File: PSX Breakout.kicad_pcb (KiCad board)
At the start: 2 copper layers, 100 x 51.8 mm, 28 parts, among them J1 Conn_01x12_Male, J2 Mini-DIN-4, J3 VAL**, J4 DB15_Female_HighDensity, J5 3x2_RCA, SW1 SW_SPDT, SW2 SW_SP3T, SW3 SW_SP3T, U1 LM1881

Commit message: Fixed Gerbers, added footprints
Updated gerbers, and added all footprints used on this board to the PSX_BREAKOUT.Pretty folder.
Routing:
- net Net-(C5-Pad1): track 84.7 -> 94.5 mm
- net GND: vias 30 -> 31
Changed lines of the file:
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@@
     (thickness 1.6)
     (drawings 18)
-    (tracks 332)
+    (tracks 334)
     (zones 0)
     (modules 28)
@@
   (page A4)
   (layers
-    (0 F.Cu signal hide)
-    (31 B.Cu signal hide)
+    (0 F.Cu signal)
+    (31 B.Cu signal)
     (32 B.Adhes user)
     (33 F.Adhes user)
@@
   (segment (start 115.443 95.377) (end 107.815 95.377) (width 0.25) (layer F.Cu) (net 8))
   (via (at 179.705 75.946) (size 0.8) (drill 0.4) (layers F.Cu B.Cu) (net 9))
-  (segment (start 124.883 86.233) (end 123.858 86.233) (width 0.25) (layer F.Cu) (net 9))
-  (segment (start 126.122 86.233) (end 124.883 86.233) (width 0.25) (layer F.Cu) (net 9))
-  (segment (start 128.513 88.624) (end 126.122 86.233) (width 0.25) (layer F.Cu) (net 9))
-  (segment (start 129.413 88.624) (end 128.513 88.624) (width 0.25) (layer F.Cu) (net 9))
-  (segment (start 120.335 91.119) (end 120.335 91.694) (width 0.25) (layer F.Cu) (net 9))
-  (segment (start 120.335 88.731) (end 120.335 91.119) (width 0.25) (layer F.Cu) (net 9))
-  (segment (start 122.833 86.233) (end 120.335 88.731) (width 0.25) (layer F.Cu) (net 9))
-  (segment (start 123.858 86.233) (end 122.833 86.233) (width 0.25) (layer F.Cu) (net 9))
   (segment (start 120.335 93.331) (end 120.321 93.345) (width 0.25) (layer F.Cu) (net 9))
   (segment (start 120.335 91.694) (end 120.335 93.331) (width 0.25) (layer F.Cu) (net 9))
@@
   (segment (start 184.418 64.897) (end 184.418 66.788) (width 0.25) (layer F.Cu) (net 9))
   (segment (start 184.418 66.788) (end 181.286989 69.919011) (width 0.25) (layer F.Cu) (net 9))
-  (segment (start 129.413 88.624) (end 130.28371 87.75329) (width 0.25) (layer F.Cu) (net 9))
-  (segment (start 139.007315 79.375) (end 139.573 79.375) (width 0.25) (layer F.Cu) (net 9))
   (via (at 139.573 79.375) (size 0.8) (drill 0.4) (layers F.Cu B.Cu) (net 9))
-  (segment (start 130.28371 87.75329) (end 130.28371 87.082605) (width 0.25) (layer F.Cu) (net 9))
-  (segment (start 137.991315 79.375) (end 139.007315 79.375) (width 0.25) (layer F.Cu) (net 9))
-  (segment (start 130.28371 87.082605) (end 137.991315 79.375) (width 0.25) (layer F.Cu) (net 9))
   (segment (start 139.972999 78.975001) (end 139.573 79.375) (width 0.25) (layer B.Cu) (net 9))
   (segment (start 140.462 78.486) (end 139.972999 78.975001) (width 0.25) (layer B.Cu) (net 9))
   (segment (start 177.165 78.486) (end 140.462 78.486) (width 0.25) (layer B.Cu) (net 9))
   (segment (start 179.705 75.946) (end 177.165 78.486) (width 0.25) (layer B.Cu) (net 9))
+  (segment (start 120.335 91.374) (end 120.335 91.694) (width 0.25) (layer F.Cu) (net 9))
+  (segment (start 122.428 89.281) (end 120.335 91.374) (width 0.25) (layer F.Cu) (net 9))
+  (segment (start 122.428 86.638) (end 122.428 89.281) (width 0.25) (layer F.Cu) (net 9))
+  (segment (start 123.858 86.233) (end 122.833 86.233) (width 0.25) (layer F.Cu) (net 9))
+  (segment (start 122.833 86.233) (end 122.428 86.638) (width 0.25) (layer F.Cu) (net 9))
+  (segment (start 129.413 87.224) (end 127.406 85.217) (width 0.25) (layer F.Cu) (net 9))
+  (segment (start 129.413 88.624) (end 129.413 87.224) (width 0.25) (layer F.Cu) (net 9))
+  (segment (start 127.406 85.217) (end 122.809 85.217) (width 0.25) (layer F.Cu) (net 9))
+  (segment (start 120.335 87.691) (end 120.335 91.694) (width 0.25) (layer F.Cu) (net 9))
+  (segment (start 122.809 85.217) (end 120.335 87.691) (width 0.25) (layer F.Cu) (net 9))
+  (segment (start 139.007315 79.375) (end 139.573 79.375) (width 0.25) (layer F.Cu) (net 9))
+  (segment (start 137.991315 79.375) (end 139.007315 79.375) (width 0.25) (layer F.Cu) (net 9))
+  (segment (start 129.413 88.624) (end 129.413 87.953315) (width 0.25) (layer F.Cu) (net 9))
+  (segment (start 129.413 87.953315) (end 137.991315 79.375) (width 0.25) (layer F.Cu) (net 9))
   (via (at 130.556 83.566) (size 0.8) (drill 0.4) (layers F.Cu B.Cu) (net 10))
   (via (at 134.874 89.154) (size 0.8) (drill 0.4) (layers F.Cu B.Cu) (net 10))
@@
   (via (at 120.523 105.791) (size 0.8) (drill 0.4) (layers F.Cu B.Cu) (net 10))
   (via (at 114.173 96.393) (size 0.8) (drill 0.4) (layers F.Cu B.Cu) (net 10))
+  (via (at 121.412 88.392) (size 0.8) (drill 0.4) (layers F.Cu B.Cu) (net 10))
   (segment (start 133.543 85.485) (end 133.529 85.471) (width 0.25) (layer F.Cu) (net 11))
   (segment (start 133.543 87.249) (end 133.543 85.485) (width 0.25) (layer F.Cu) (net 11))

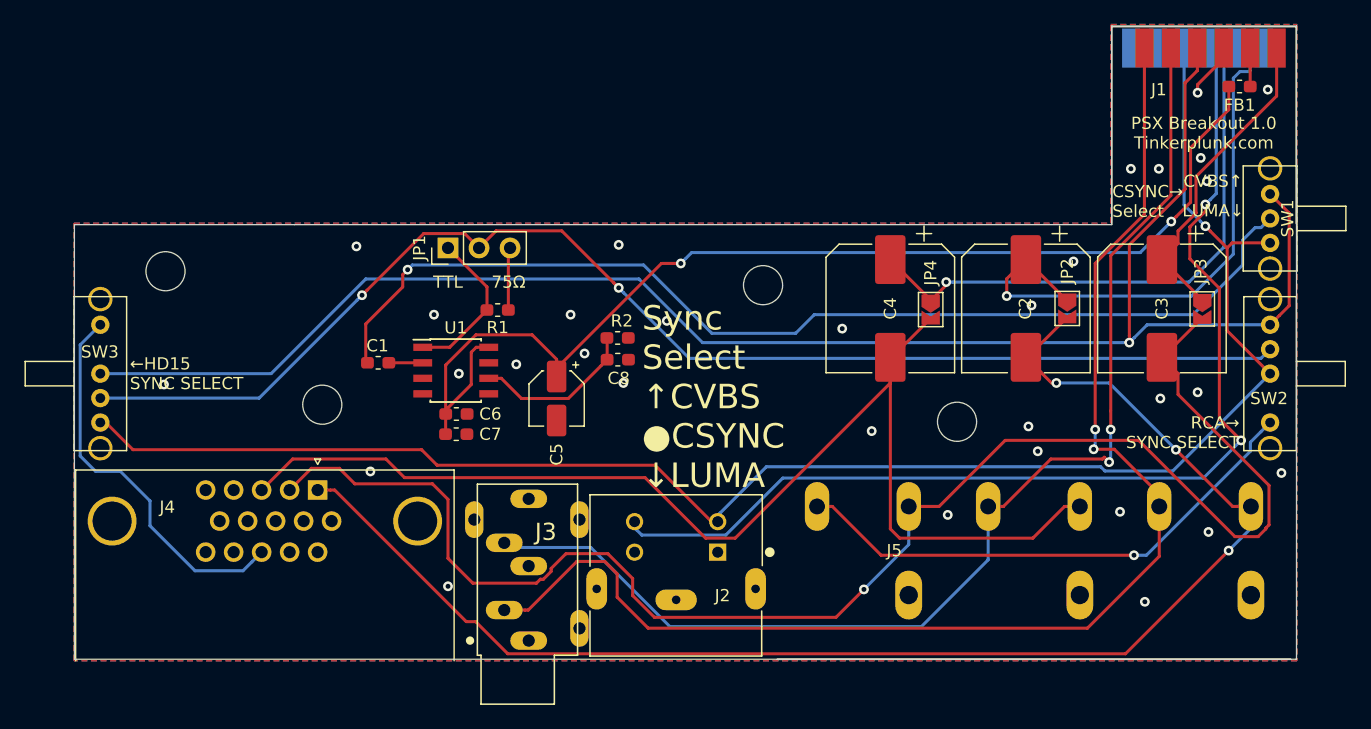
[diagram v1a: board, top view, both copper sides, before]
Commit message: Fixed s-video and headphone footprint, added support hole
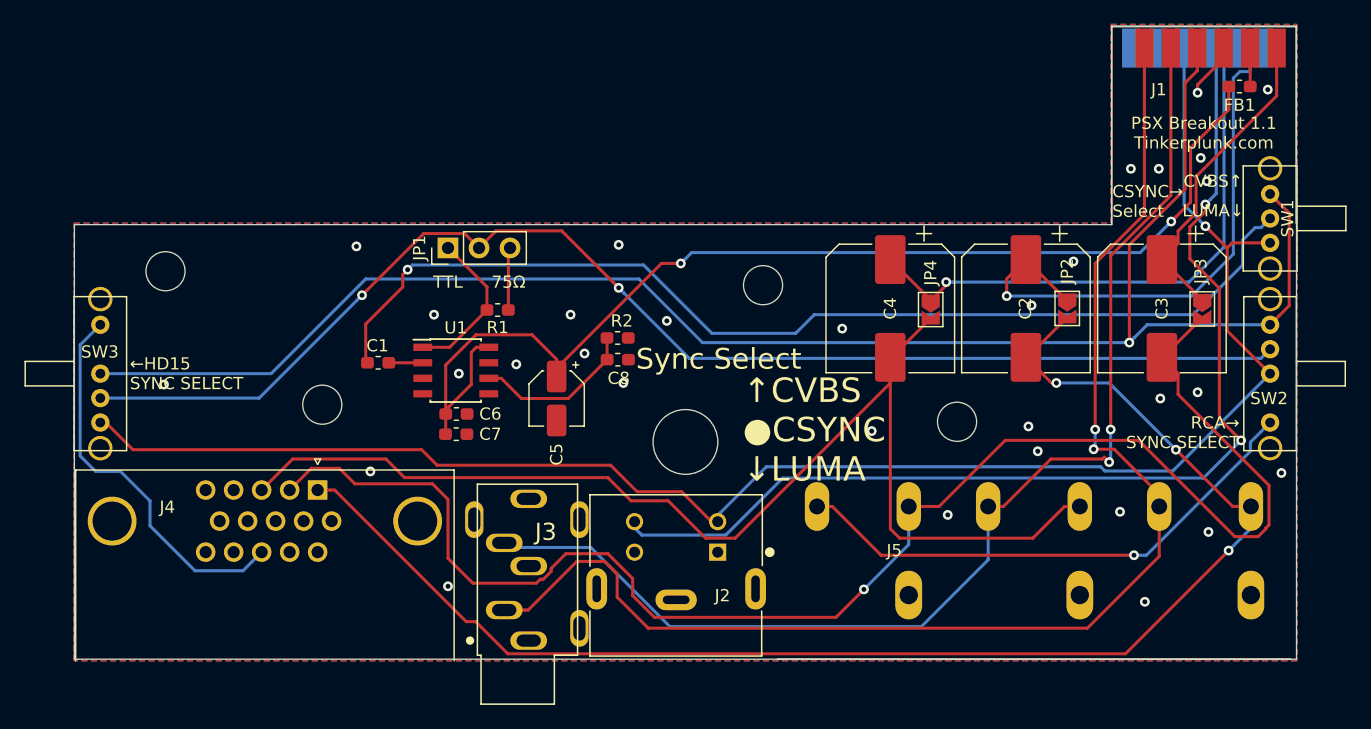
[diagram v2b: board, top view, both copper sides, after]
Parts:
- added REF**: MountingHole_5.3mm_M5, MountingHole:MountingHole_5.3mm_M5, F.Cu at (140.0, 94.0)
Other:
- board text added: "PSX Breakout 1.1 Tinkerplunk.com"
- board text added: "Sync Select"
- board text added: "↑CVBS ●CSYNC ↓LUMA"
- board text removed: "PSX Breakout 1.0 Tinkerplunk.com"
- board text removed: "Sync Select ↑CVBS ●CSYNC ↓LUMA"

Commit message: Updated to 1.2
Removed sync stripper, shrunk board, added switch to select sync source of HD15 port only.
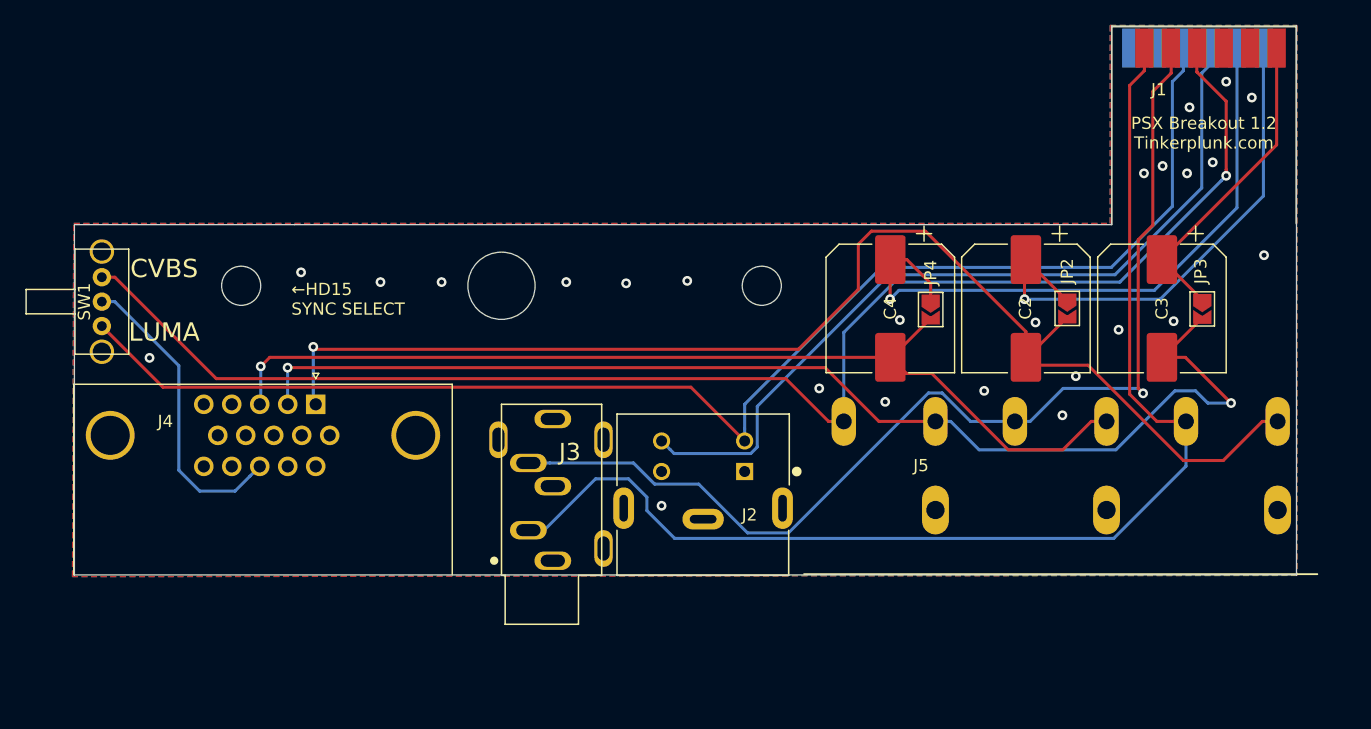
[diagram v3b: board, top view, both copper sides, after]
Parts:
- removed C1, C6, C8: 100nF, Capacitor_SMD:C_0603_1608Metric_Pad1.05x0.95mm_HandSolder
- removed C5: 10uF, Capacitor_SMD:CP_Elec_4x5.4
- removed C7: 10nF, Capacitor_SMD:C_0603_1608Metric_Pad1.05x0.95mm_HandSolder
- removed FB1: 220R, Inductor_SMD:L_0603_1608Metric_Pad1.05x0.95mm_HandSolder
- removed JP1: Jumper_3_Open, Connector_PinHeader_2.54mm:PinHeader_1x03_P2.54mm_Vertical
- removed R1: 470, Resistor_SMD:R_0603_1608Metric_Pad1.05x0.95mm_HandSolder
- removed R2: 680K, Resistor_SMD:R_0603_1608Metric_Pad1.05x0.95mm_HandSolder
- removed the REF** at (140.0, 94.0)
- removed the REF** at (110.2, 90.9)
- removed the REF** at (97.4, 80.0)
- removed the REF** at (162.2, 92.3)
- removed the REF** at (146.3, 81.2)
- removed SW2, SW3: SW_SP3T, PSX_BREAKOUT:C&K_SP3T
- removed U1: LM1881, Package_SO:SOIC-8_3.9x4.9mm_P1.27mm
- added REF**: MountingHole_5.5mm, MountingHole:MountingHole_5.5mm, F.Cu at (124.9, 81.2)
- added REF**: MountingHole_3.2mm_M3, MountingHole:MountingHole_3.2mm_M3, F.Cu at (103.6, 81.2)
- added REF**: MountingHole_3.2mm_M3, MountingHole:MountingHole_3.2mm_M3, F.Cu at (146.2, 81.2)
- J3: value VAL** -> AudioJack3; footprint SJ1-3533NG:CUI_SJ1-3533NG -> Tinkerplunk:CUI_SJ1-3533NG
- J4: footprint Connector_Dsub:DSUB-15-HD_Female_Horizontal_P2.29x1.98mm_EdgePinOffset8.35mm_Housed_MountingHolesOffset10.89mm -> Tinkerplunk:VGA
- SW1: footprint PSX_BREAKOUT:C&K_SPDT -> Tinkerplunk:C&K_SPDT
- moved SW1 95.8 mm to (92.2, 82.5), turned to 270 degrees
- moved J5 7.30 mm to (170.7, 104.8)
- moved J4 7.02 mm to (109.7, 90.9)
- moved J2 6.96 mm to (141.4, 98.3)
- moved J3 6.83 mm to (129.1, 103.7)
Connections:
- J2 pad S1: GND -> (no net)
- J2 pad S2: GND -> (no net)
- J2 pad S3: GND -> (no net)
- J5 pad 1: RCA_SYNC_OUT -> CVBS
- SW1 pad 1: LUMA -> CVBS
- SW1 pad 2: Net-(C1-Pad2) -> VGA_SYNC_OUT
- SW1 pad 3: CVBS -> LUMA
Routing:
- net CSYNC: track 107.0 -> 0.00 mm, vias 2 -> 0
- net Net-(C5-Pad1): track 94.5 -> 0.00 mm, vias 2 -> 0
- net Net-(C1-Pad2): track 87.2 -> 0.00 mm, vias 1 -> 0
- net RCA_SYNC_OUT: track 43.7 -> 0.00 mm, vias 1 -> 0
- net GREEN_OUT: track 125.2 -> 97.3 mm, vias 1 -> 2
- net LUMA: track 137.6 -> 114.6 mm, vias 1 -> 0
- net CHROMA: track 88.7 -> 65.7 mm, vias 2 -> 0
- net CVBS: track 140.1 -> 120.9 mm
- net BLUE_OUT: track 98.1 -> 81.4 mm, vias 0 -> 1
- net RED_OUT: track 119.3 -> 105.4 mm, vias 3 -> 1
- net Net-(C8-Pad1): track 13.5 -> 0.00 mm
- net Net-(JP1-Pad1): track 12.9 -> 0.00 mm
- net RIGHT: track 108.1 -> 98.7 mm, vias 2 -> 0
- net LEFT: track 97.3 -> 89.2 mm, vias 2 -> 1
- net VGA_SYNC_OUT: track 32.0 -> 25.2 mm
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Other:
- board size 100 x 51.8 mm -> 100 x 44.9 mm
- board text added: "CVBS"
- board text added: "LUMA"
- board text added: "PSX Breakout 1.2 Tinkerplunk.com"
- board text removed: "75Ω"
- board text removed: "CSYNC→ Select"
- board text removed: "CVBS↑"
- board text removed: "LUMA↓"
- board text removed: "PSX Breakout 1.1 Tinkerplunk.com"
- board text removed: "RCA→ SYNC SELECT"
- board text removed: "Sync Select"
- board text removed: "TTL"
- board text removed: "↑CVBS ●CSYNC ↓LUMA"
